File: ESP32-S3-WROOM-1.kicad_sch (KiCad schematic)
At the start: 24 parts, among them J11 Conn_01x08, J13 Conn_02x09_Top_Bottom, J14 Conn_01x09, J15 Conn_02x09_Top_Bottom, J4 B4B-ZRLFSN, J6 Conn_01x09, J7 Conn_02x20_Counter_Clockwise, J8 Conn_01x08, J9 Conn_01x08, SW4 SW_Push, U8 ESP32-S3-WROOM-1-N8R2

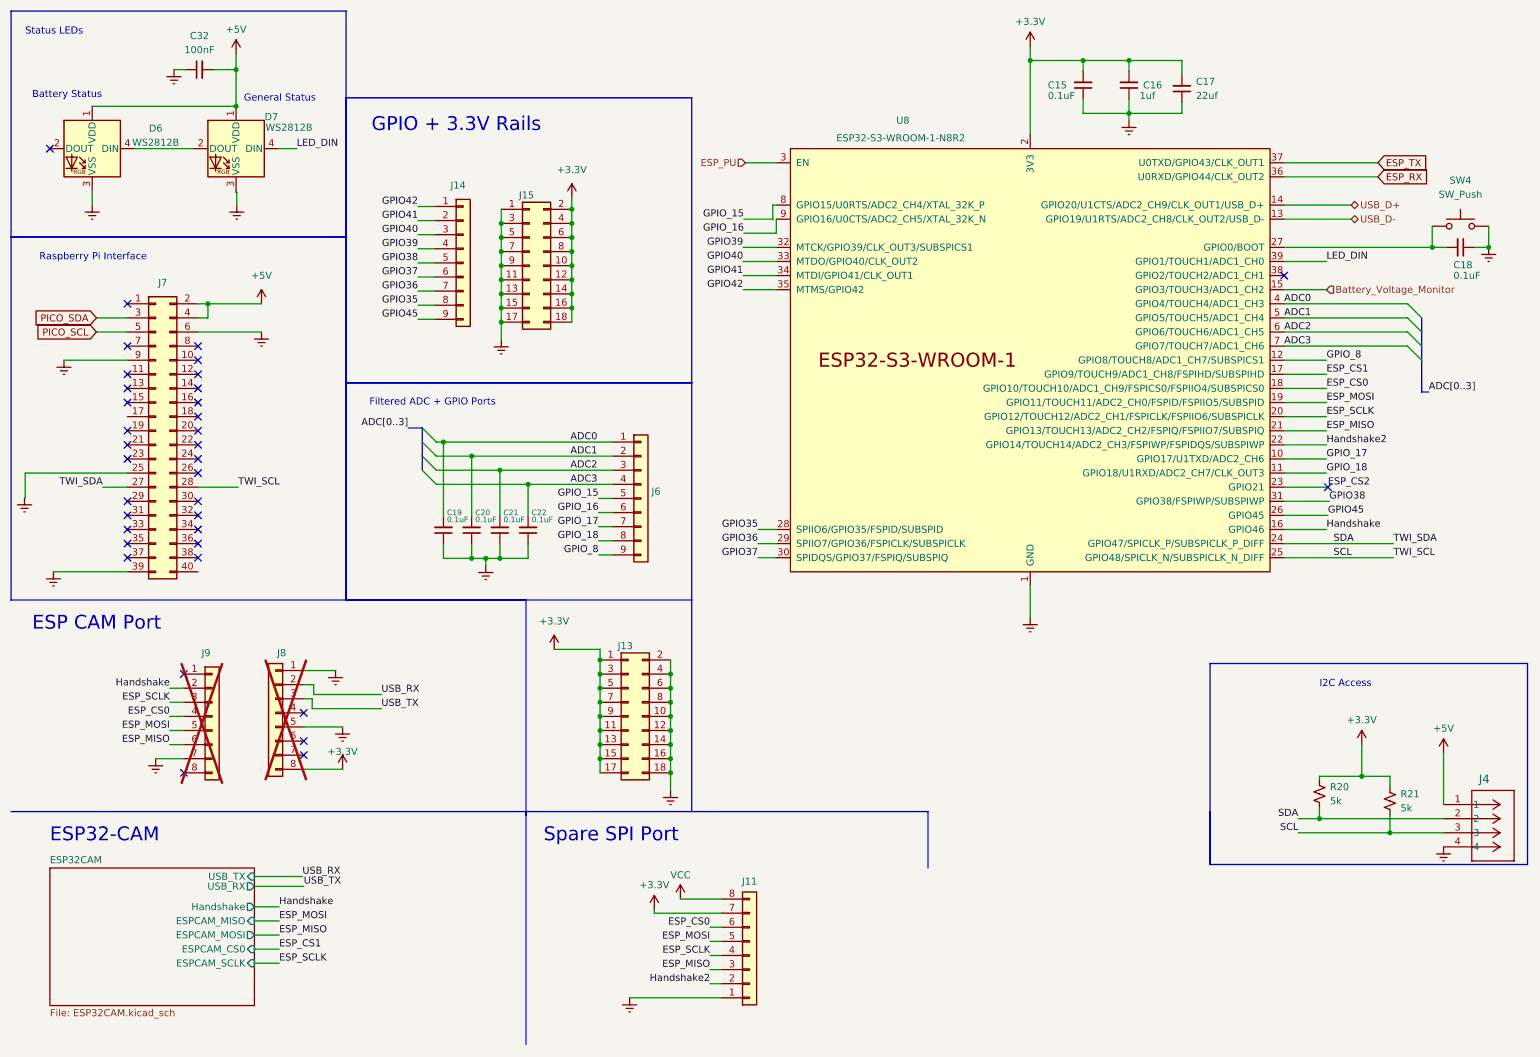
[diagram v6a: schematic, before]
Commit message: update to I2C
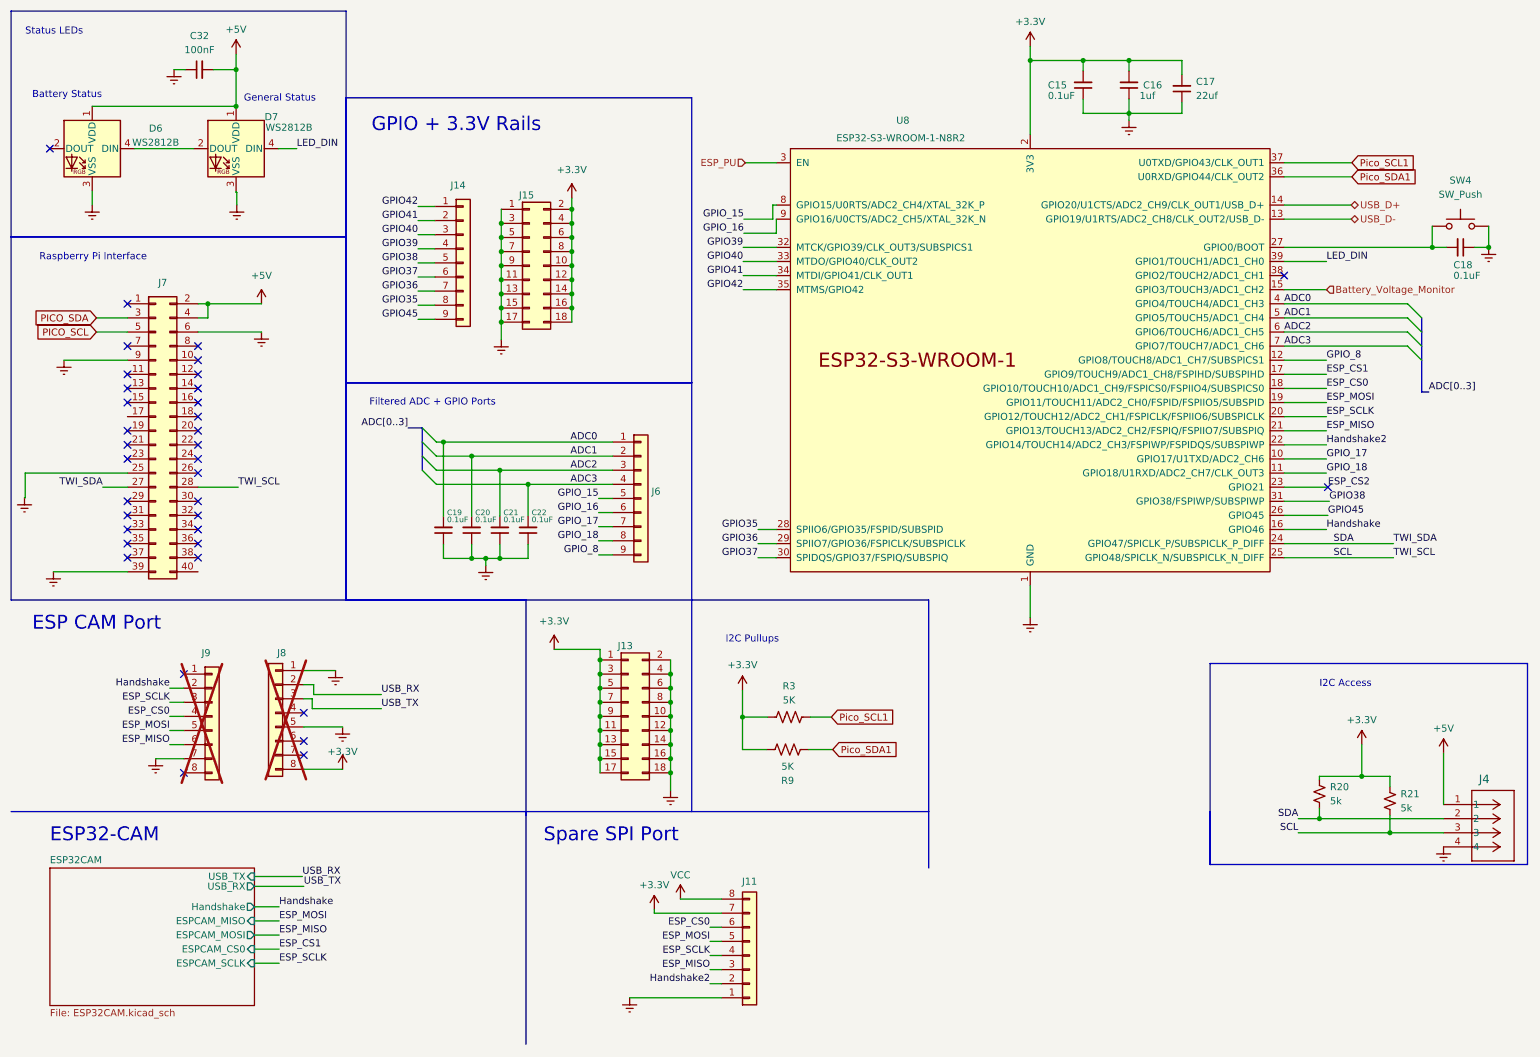
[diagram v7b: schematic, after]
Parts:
- added R3, R9: 5K, Resistor_SMD:R_0402_1005Metric, symbol Device:R_US
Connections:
- net +3.3V: now also R3.1, R9.2
- net ESP_RX renamed Pico_SDA1
- net Pico_SDA1: now also R9.1
- net ESP_TX renamed Pico_SCL1
- net Pico_SCL1: now also R3.2
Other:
- note added: "I2C Pullups"
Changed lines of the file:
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@@
   (junction (at 117.856 131.191) (diameter 0) (color 0 0 0 0)
+  )
+  (junction (at 143.51 138.938) (diameter 0) (color 0 0 0 0)
   )
   (no_connect (at 32.766 107.696))
@@
     (stroke (width 0) (type default))
   )
+  (wire (pts (xy 148.082 138.938) (xy 143.51 138.938))
+    (stroke (width 0) (type default))
+  )
   (wire (pts (xy 130.556 133.731) (xy 130.556 136.271))
     (stroke (width 0) (type default))
@@
     (stroke (width 0) (type default))
   )
-  (polyline (pts (xy 176.911 166.116) (xy 176.911 155.956))
+  (polyline (pts (xy 177.038 166.116) (xy 177.038 155.956))
     (stroke (width 0) (type default))
   )
@@
     (stroke (width 0) (type default))
   )
+  (wire (pts (xy 155.448 144.78) (xy 159.766 144.78))
+    (stroke (width 0) (type default))
+  )
   (wire (pts (xy 222.631 20.701) (xy 222.631 23.241))
     (stroke (width 0) (type default))
@@
     (stroke (width 0) (type default))
   )
+  (polyline (pts (xy 134.366 117.856) (xy 177.038 117.856))
+    (stroke (width 0) (type default))
+  )
   (wire (pts (xy 48.26 22.352) (xy 52.324 22.352))
     (stroke (width 0) (type default))
@@
     (stroke (width 0) (type default))
   )
+  (wire (pts (xy 143.51 144.78) (xy 147.828 144.78))
+    (stroke (width 0) (type default))
+  )
   (wire (pts (xy 248.666 82.296) (xy 241.046 82.296))
     (stroke (width 0) (type default))
@@
     (stroke (width 0) (type default))
   )
+  (polyline (pts (xy 177.038 117.856) (xy 177.038 155.956))
+    (stroke (width 0) (type default))
+  )
   (wire (pts (xy 130.556 152.146) (xy 130.556 148.971))
     (stroke (width 0) (type default))
@@
     (stroke (width 0) (type default))
   )
+  (wire (pts (xy 159.512 138.938) (xy 155.702 138.938))
+    (stroke (width 0) (type default))
+  )
   (wire (pts (xy 248.666 87.376) (xy 241.046 87.376))
     (stroke (width 0) (type default))
@@
     (stroke (width 0) (type default))
   )
-  (wire (pts (xy 241.046 41.656) (xy 257.937 41.656))
+  (wire (pts (xy 241.046 41.656) (xy 253.238 41.656))
     (stroke (width 0) (type default))
   )
@@
     (stroke (width 0) (type default))
   )
-  (polyline (pts (xy 176.911 155.956) (xy 104.521 155.956))
+  (polyline (pts (xy 177.038 155.956) (xy 104.521 155.956))
     (stroke (width 0) (type default))
   )
@@
     (stroke (width 0) (type default))
   )
+  (wire (pts (xy 143.51 138.938) (xy 143.51 134.112))
+    (stroke (width 0) (type default))
+  )
   (wire (pts (xy 137.668 179.324) (xy 139.7 179.324))
     (stroke (width 0) (type default))
@@
     (stroke (width 0) (type default))
   )
+  (wire (pts (xy 143.51 138.938) (xy 143.51 144.78))
+    (stroke (width 0) (type default))
+  )
   (wire (pts (xy 204.851 20.701) (xy 204.851 22.606))
     (stroke (width 0) (type default))
@@
     (stroke (width 0) (type default))
   )
-  (wire (pts (xy 241.046 39.116) (xy 257.937 39.116))
+  (wire (pts (xy 241.046 39.116) (xy 253.238 39.116))
     (stroke (width 0) (type default))
   )
@@
     (effects (font (size 1.27 1.27)) (justify left bottom))
   )
+  (text "I2C Pullups" (at 140.462 125.73 0)
+    (effects (font (size 1.27 1.27)) (justify left bottom))
+  )
   (text "ESP32-CAM" (at 18.796 161.671 0)
     (effects (font (size 2.5 2.5)) (justify left bottom))
@@
     (effects (font (size 1.27 1.27)) (justify right bottom))
   )
-  (global_label "ESP_RX" (shape input) (at 257.937 41.656 0) (fields_autoplaced)
+  (global_label "Pico_SDA1" (shape input) (at 159.766 144.78 0) (fields_autoplaced)
     (effects (font (size 1.27 1.27)) (justify left))
-    (property "Intersheetrefs" "${INTERSHEET_REFS}" (at 267.9978 41.656 0)
+    (property "Intersheetrefs" "${INTERSHEET_REFS}" (at 172.6088 144.78 0)
       (effects (font (size 1.27 1.27)) (justify left) hide)
     )
   )
-  (global_label "ESP_TX" (shape input) (at 257.937 39.116 0) (fields_autoplaced)
+  (global_label "Pico_SDA1" (shape input) (at 253.238 41.656 0) (fields_autoplaced)
     (effects (font (size 1.27 1.27)) (justify left))
-    (property "Intersheetrefs" "${INTERSHEET_REFS}" (at 267.6954 39.116 0)
+    (property "Intersheetrefs" "${INTERSHEET_REFS}" (at 266.0808 41.656 0)
+      (effects (font (size 1.27 1.27)) (justify left) hide)
+    )
+  )
+  (global_label "Pico_SCL1" (shape input) (at 159.512 138.938 0) (fields_autoplaced)
+    (effects (font (size 1.27 1.27)) (justify left))
+    (property "Intersheetrefs" "${INTERSHEET_REFS}" (at 172.2943 138.938 0)
+      (effects (font (size 1.27 1.27)) (justify left) hide)
+    )
+  )
+  (global_label "Pico_SCL1" (shape input) (at 253.238 39.116 0) (fields_autoplaced)
+    (effects (font (size 1.27 1.27)) (justify left))
+    (property "Intersheetrefs" "${INTERSHEET_REFS}" (at 266.0203 39.116 0)
       (effects (font (size 1.27 1.27)) (justify left) hide)
     )
@@
         (path "/cced1a6d-3dc4-42b2-93bd-998a7b4cf4e8/5eb80655-957d-4a1c-8d7d-b2e173715026"
           (reference "#PWR070") (unit 1)
+        )
+      )
+    )
+  )
+  (symbol (lib_id "Device:R_US") (at 151.892 138.938 90) (unit 1)
+    (in_bom yes) (on_board yes) (dnp no) (fields_autoplaced)
+    (property "Reference" "R3" (at 151.892 133.35 90)
+      (effects (font (size 1.27 1.27)))
+    )
+    (property "Value" "5K" (at 151.892 135.89 90)
+      (effects (font (size 1.27 1.27)))
+    )
+    (property "Footprint" "Resistor_SMD:R_0402_1005Metric" (at 152.146 137.922 90)
+      (effects (font (size 1.27 1.27)) hide)
+    )
+    (property "Datasheet" "~" (at 151.892 138.938 0)
+      (effects (font (size 1.27 1.27)) hide)
+    )
+    (pin "1")
+    (pin "2")
+    (instances
+      (project "DeltaRhoRobot"
+        (path "/cced1a6d-3dc4-42b2-93bd-998a7b4cf4e8/5eb80655-957d-4a1c-8d7d-b2e173715026"
+          (reference "R3") (unit 1)
         )
       )
@@
     )
   )
+  (symbol (lib_id "Device:R_US") (at 151.638 144.78 270) (unit 1)
+    (in_bom yes) (on_board yes) (dnp no)
+    (property "Reference" "R9" (at 151.638 150.368 90)
+      (effects (font (size 1.27 1.27)))
+    )
+    (property "Value" "5K" (at 151.638 147.828 90)
+      (effects (font (size 1.27 1.27)))
+    )
+    (property "Footprint" "Resistor_SMD:R_0402_1005Metric" (at 151.384 145.796 90)
+      (effects (font (size 1.27 1.27)) hide)
+    )
+    (property "Datasheet" "~" (at 151.638 144.78 0)
+      (effects (font (size 1.27 1.27)) hide)
+    )
+    (pin "1")
+    (pin "2")
+    (instances
+      (project "DeltaRhoRobot"
+        (path "/cced1a6d-3dc4-42b2-93bd-998a7b4cf4e8/5eb80655-957d-4a1c-8d7d-b2e173715026"
+          (reference "R9") (unit 1)
+        )
+      )
+    )
+  )
   (symbol (lib_id "power:Earth") (at 213.106 31.496 0) (unit 1)
     (in_bom yes) (on_board yes) (dnp no) (fields_autoplaced)
@@
         )
       )
+    )
+  )
+  (symbol (lib_id "power:+3.3V") (at 143.51 134.112 0) (unit 1)
+    (in_bom yes) (on_board yes) (dnp no) (fields_autoplaced)
+    (property "Reference" "#PWR0123" (at 143.51 137.922 0)
+      (effects (font (size 1.27 1.27)) hide)
+    )
+    (property "Value" "+3.3V" (at 143.51 129.54 0)
+      (effects (font (size 1.27 1.27)))
+    )
+    (property "Footprint" "" (at 143.51 134.112 0)
+      (effects (font (size 1.27 1.27)) hide)
+    )
+    (property "Datasheet" "" (at 143.51 134.112 0)
+      (effects (font (size 1.27 1.27)) hide)
+    )
+    (pin "1")
+    (instances
+      (project "DeltaRhoRobot"
+        (path "/cced1a6d-3dc4-42b2-93bd-998a7b4cf4e8/5eb80655-957d-4a1c-8d7d-b2e173715026"
+          (reference "#PWR0123") (unit 1)
+        )
+      )

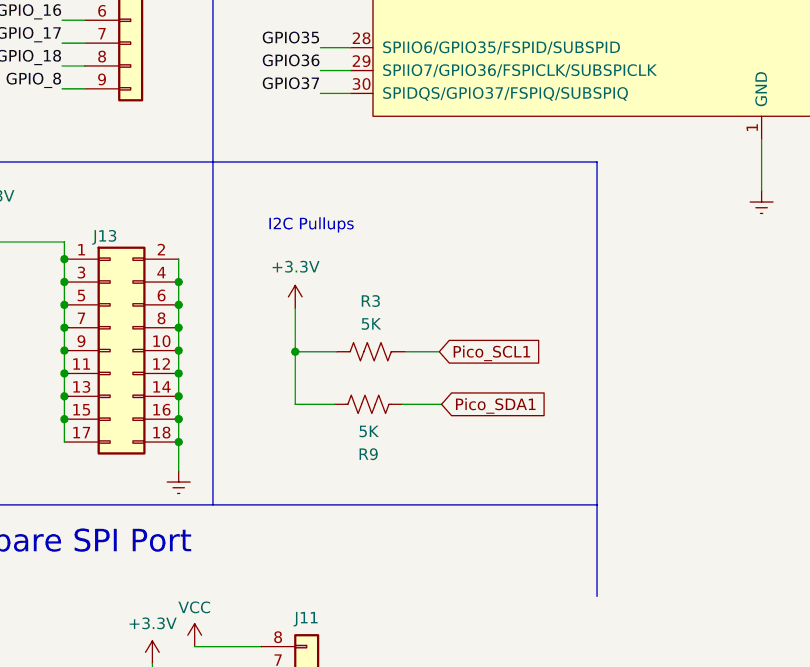
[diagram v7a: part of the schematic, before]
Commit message: Fixed resistors
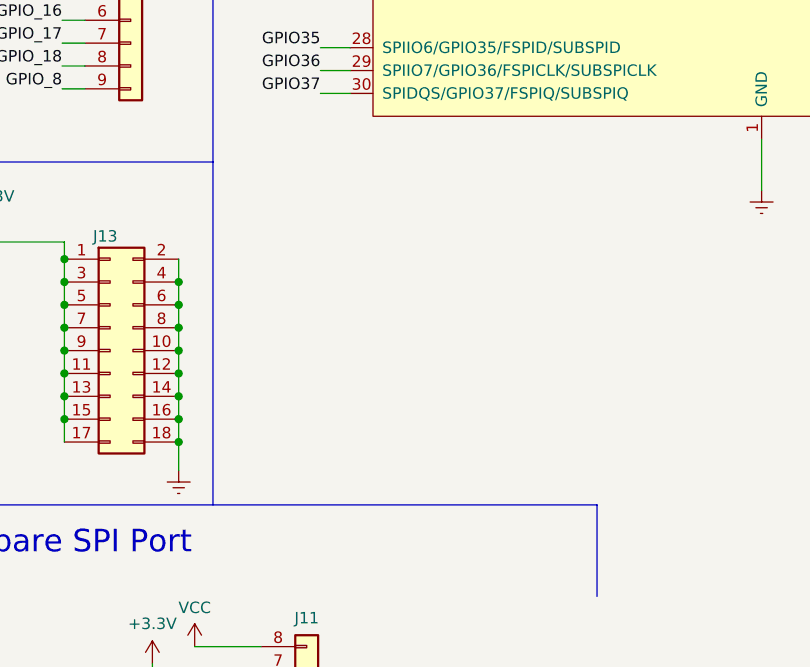
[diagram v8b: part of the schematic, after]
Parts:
- removed R3, R9: 5K, Resistor_SMD:R_0402_1005Metric, symbol Device:R_US
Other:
- note removed: "I2C Pullups"
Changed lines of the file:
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@@
   (junction (at 117.856 131.191) (diameter 0) (color 0 0 0 0)
-  )
-  (junction (at 143.51 138.938) (diameter 0) (color 0 0 0 0)
   )
   (no_connect (at 32.766 107.696))
@@
     (stroke (width 0) (type default))
   )
-  (wire (pts (xy 148.082 138.938) (xy 143.51 138.938))
-    (stroke (width 0) (type default))
-  )
   (wire (pts (xy 130.556 133.731) (xy 130.556 136.271))
     (stroke (width 0) (type default))
@@
     (stroke (width 0) (type default))
   )
-  (wire (pts (xy 155.448 144.78) (xy 159.766 144.78))
-    (stroke (width 0) (type default))
-  )
   (wire (pts (xy 222.631 20.701) (xy 222.631 23.241))
     (stroke (width 0) (type default))
@@
     (stroke (width 0) (type default))
   )
-  (polyline (pts (xy 134.366 117.856) (xy 177.038 117.856))
-    (stroke (width 0) (type default))
-  )
   (wire (pts (xy 48.26 22.352) (xy 52.324 22.352))
     (stroke (width 0) (type default))
@@
     (stroke (width 0) (type default))
   )
-  (wire (pts (xy 143.51 144.78) (xy 147.828 144.78))
-    (stroke (width 0) (type default))
-  )
   (wire (pts (xy 248.666 82.296) (xy 241.046 82.296))
     (stroke (width 0) (type default))
@@
     (stroke (width 0) (type default))
   )
-  (polyline (pts (xy 177.038 117.856) (xy 177.038 155.956))
-    (stroke (width 0) (type default))
-  )
   (wire (pts (xy 130.556 152.146) (xy 130.556 148.971))
     (stroke (width 0) (type default))
@@
     (stroke (width 0) (type default))
   )
-  (wire (pts (xy 159.512 138.938) (xy 155.702 138.938))
-    (stroke (width 0) (type default))
-  )
   (wire (pts (xy 248.666 87.376) (xy 241.046 87.376))
     (stroke (width 0) (type default))
@@
     (stroke (width 0) (type default))
   )
-  (wire (pts (xy 143.51 138.938) (xy 143.51 134.112))
-    (stroke (width 0) (type default))
-  )
   (wire (pts (xy 137.668 179.324) (xy 139.7 179.324))
     (stroke (width 0) (type default))
@@
   )
   (polyline (pts (xy 72.136 117.856) (xy 104.521 117.856))
-    (stroke (width 0) (type default))
-  )
-  (wire (pts (xy 143.51 138.938) (xy 143.51 144.78))
     (stroke (width 0) (type default))
   )
@@
     (effects (font (size 1.27 1.27)) (justify left bottom))
   )
-  (text "I2C Pullups" (at 140.462 125.73 0)
-    (effects (font (size 1.27 1.27)) (justify left bottom))
-  )
   (text "ESP32-CAM" (at 18.796 161.671 0)
     (effects (font (size 2.5 2.5)) (justify left bottom))
@@
   (label "ADC[0..3]" (at 83.312 86.868 180) (fields_autoplaced)
     (effects (font (size 1.27 1.27)) (justify right bottom))
-  )
-  (global_label "Pico_SDA1" (shape input) (at 159.766 144.78 0) (fields_autoplaced)
-    (effects (font (size 1.27 1.27)) (justify left))
-    (property "Intersheetrefs" "${INTERSHEET_REFS}" (at 172.6088 144.78 0)
-      (effects (font (size 1.27 1.27)) (justify left) hide)
-    )
   )
   (global_label "Pico_SDA1" (shape input) (at 253.238 41.656 0) (fields_autoplaced)
@@
     )
   )
-  (global_label "Pico_SCL1" (shape input) (at 159.512 138.938 0) (fields_autoplaced)
-    (effects (font (size 1.27 1.27)) (justify left))
-    (property "Intersheetrefs" "${INTERSHEET_REFS}" (at 172.2943 138.938 0)
-      (effects (font (size 1.27 1.27)) (justify left) hide)
-    )
-  )
   (global_label "Pico_SCL1" (shape input) (at 253.238 39.116 0) (fields_autoplaced)
     (effects (font (size 1.27 1.27)) (justify left))
@@
         (path "/cced1a6d-3dc4-42b2-93bd-998a7b4cf4e8/5eb80655-957d-4a1c-8d7d-b2e173715026"
           (reference "#PWR070") (unit 1)
-        )
-      )
-    )
-  )
-  (symbol (lib_id "Device:R_US") (at 151.892 138.938 90) (unit 1)
-    (in_bom yes) (on_board yes) (dnp no) (fields_autoplaced)
-    (property "Reference" "R3" (at 151.892 133.35 90)
-      (effects (font (size 1.27 1.27)))
-    )
-    (property "Value" "5K" (at 151.892 135.89 90)
-      (effects (font (size 1.27 1.27)))
-    )
-    (property "Footprint" "Resistor_SMD:R_0402_1005Metric" (at 152.146 137.922 90)
-      (effects (font (size 1.27 1.27)) hide)
-    )
-    (property "Datasheet" "~" (at 151.892 138.938 0)
-      (effects (font (size 1.27 1.27)) hide)
-    )
-    (pin "1")
-    (pin "2")
-    (instances
-      (project "DeltaRhoRobot"
-        (path "/cced1a6d-3dc4-42b2-93bd-998a7b4cf4e8/5eb80655-957d-4a1c-8d7d-b2e173715026"
-          (reference "R3") (unit 1)
         )
       )
@@
     )
   )
-  (symbol (lib_id "Device:R_US") (at 151.638 144.78 270) (unit 1)
-    (in_bom yes) (on_board yes) (dnp no)
-    (property "Reference" "R9" (at 151.638 150.368 90)
-      (effects (font (size 1.27 1.27)))
-    )
-    (property "Value" "5K" (at 151.638 147.828 90)
-      (effects (font (size 1.27 1.27)))
-    )
-    (property "Footprint" "Resistor_SMD:R_0402_1005Metric" (at 151.384 145.796 90)
-      (effects (font (size 1.27 1.27)) hide)
-    )
-    (property "Datasheet" "~" (at 151.638 144.78 0)
-      (effects (font (size 1.27 1.27)) hide)
-    )
-    (pin "1")
-    (pin "2")
-    (instances
-      (project "DeltaRhoRobot"
-        (path "/cced1a6d-3dc4-42b2-93bd-998a7b4cf4e8/5eb80655-957d-4a1c-8d7d-b2e173715026"
-          (reference "R9") (unit 1)
-        )
-      )
-    )
-  )
   (symbol (lib_id "power:Earth") (at 213.106 31.496 0) (unit 1)
     (in_bom yes) (on_board yes) (dnp no) (fields_autoplaced)
@@
         )
       )
-    )
-  )
-  (symbol (lib_id "power:+3.3V") (at 143.51 134.112 0) (unit 1)
-    (in_bom yes) (on_board yes) (dnp no) (fields_autoplaced)
-    (property "Reference" "#PWR0123" (at 143.51 137.922 0)
-      (effects (font (size 1.27 1.27)) hide)
-    )
-    (property "Value" "+3.3V" (at 143.51 129.54 0)
-      (effects (font (size 1.27 1.27)))
-    )
-    (property "Footprint" "" (at 143.51 134.112 0)
-      (effects (font (size 1.27 1.27)) hide)
-    )
-    (property "Datasheet" "" (at 143.51 134.112 0)
-      (effects (font (size 1.27 1.27)) hide)
-    )
-    (pin "1")
-    (instances
-      (project "DeltaRhoRobot"
-        (path "/cced1a6d-3dc4-42b2-93bd-998a7b4cf4e8/5eb80655-957d-4a1c-8d7d-b2e173715026"
-          (reference "#PWR0123") (unit 1)
-        )
-      )
